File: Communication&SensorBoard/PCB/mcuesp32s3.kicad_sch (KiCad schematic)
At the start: 10 parts, among them J6 Conn_01x03, SW1 SW_Push, SW2 SW_SPDT, U2 ESP32-S3-MINI-1U

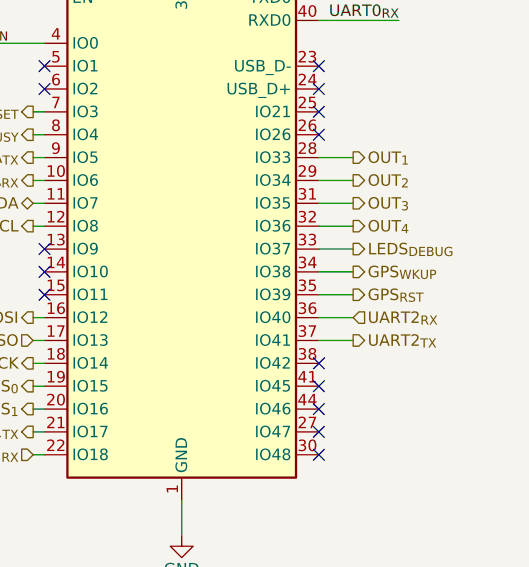
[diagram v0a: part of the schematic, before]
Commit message: C&S board - update GPS
se cambio el conector del gps pasando de un sistema incorporado en placa a un sistema externo, con el BZ251
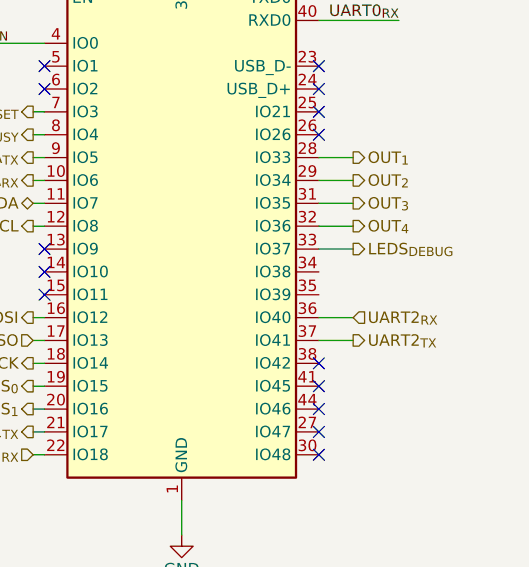
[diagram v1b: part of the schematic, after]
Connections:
- net GPS_{RST}: no longer names the net of U2.35 (IO39)
- net GPS_{WKUP}: no longer names the net of U2.34 (IO38)
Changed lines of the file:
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@@
 	(wire
 		(pts
-			(xy 173.99 62.23) (xy 170.18 62.23)
+			(xy 48.26 68.58) (xy 44.45 68.58)
 		)
 		(stroke
@@
 		)
 	)
-	(wire
-		(pts
-			(xy 48.26 68.58) (xy 44.45 68.58)
-		)
-		(stroke
-			(width 0)
-			(type default)
-		)
-	)
 	(polyline
 		(pts
@@
 		)
 	)
-	(wire
-		(pts
-			(xy 173.99 64.77) (xy 170.18 64.77)
-		)
-		(stroke
-			(width 0)
-			(type default)
-		)
-	)
 	(label "ESP32_{BOOT}"
 		(at 60.96 68.58 180)
@@
 		)
 	)
-	(hierarchical_label "GPS_{RST}"
-		(shape output)
-		(at 173.99 64.77 0)
-		(effects
-			(font
-				(size 1.27 1.27)
-			)
-			(justify left)
-		)
-	)
 	(hierarchical_label "UART1_{TX}"
 		(shape output)
@@
 		(effects
 			(font
-				(size 1.27 1.27)
-			)
-			(justify left)
-		)
-	)
-	(hierarchical_label "GPS_{WKUP}"
-		(shape output)
-		(at 173.99 62.23 0)
-		(effects
-			(font
